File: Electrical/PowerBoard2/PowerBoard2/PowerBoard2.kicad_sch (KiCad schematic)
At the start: 10 parts, among them J1 XT60PW-M, J2 XT60PW-M, J3 B4B-XH-A_LF__SN_, J5 XT60PW-M, U2 INA226AIDGSR, U3 USB-A-S-RA-TSMT

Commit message: pullup resistors
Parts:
- R3, R4: footprint (none) -> Resistor_SMD:R_0805_2012Metric_Pad1.20x1.40mm_HandSolder
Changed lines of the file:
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@@
 			)
 		)
-		(property "Footprint" ""
+		(property "Footprint" "Resistor_SMD:R_0805_2012Metric_Pad1.20x1.40mm_HandSolder"
 			(at 58.42 90.678 90)
 			(effects
@@
 			)
 		)
-		(property "Footprint" ""
+		(property "Footprint" "Resistor_SMD:R_0805_2012Metric_Pad1.20x1.40mm_HandSolder"
 			(at 58.42 85.598 90)
 			(effects

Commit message: widened traces for 5V output
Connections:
- net +3.3V: now reaches J3.1, R3.1, R4.1, U2.6 (VS)
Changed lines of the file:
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@@
+	)
+	(junction
+		(at 123.19 74.93)
+		(diameter 0)
+		(color 0 0 0 0)
 	)
 	(junction
@@
 	(wire
 		(pts
+			(xy 123.19 74.93) (xy 111.76 74.93)
+		)
+		(stroke
+			(width 0)
+			(type default)
+		)
+	)
+	(wire
+		(pts
 			(xy 104.14 68.58) (xy 114.3 68.58)
 		)
@@
 	(wire
 		(pts
-			(xy 128.27 74.93) (xy 111.76 74.93)
+			(xy 128.27 74.93) (xy 123.19 74.93)
 		)
 		(stroke
@@
 					(unit 1)
 				)
+			)
+		)
+	)
+	(symbol
+		(lib_id "power:+3.3V")
+		(at 123.19 74.93 0)
+		(unit 1)
+		(exclude_from_sim no)
+		(in_bom yes)
+		(on_board yes)
+		(dnp no)
+		(fields_autoplaced yes)
+		(property "Reference" "#PWR011"
+			(at 123.19 78.74 0)
+			(effects
+				(font
+					(size 1.27 1.27)
+				)
+				(hide yes)
+			)
+		)
+		(property "Value" "+3.3V"
+			(at 123.19 69.85 0)
+			(effects
+				(font
+					(size 1.27 1.27)
+				)
+			)
+		)
+		(property "Footprint" ""
+			(at 123.19 74.93 0)
+			(effects
+				(font
+					(size 1.27 1.27)
+				)
+				(hide yes)
+			)
+		)
+		(property "Datasheet" ""
+			(at 123.19 74.93 0)
+			(effects
+				(font
+					(size 1.27 1.27)
+				)
+				(hide yes)
+			)
+		)
+		(property "Description" "Power symbol creates a global label with name \"+3.3V\""
+			(at 123.19 74.93 0)
+			(effects
+				(font
+					(size 1.27 1.27)
+				)
+				(hide yes)
+			)
+		)
+		(pin "1"
+		)
+		(instances
+			(project ""
+				(path "/f95f296f-a4bf-4952-bdc7-66087a6cc347"
+					(reference "#PWR011")
+					(unit 1)
+				)

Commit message: stabilizing capacitors
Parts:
- added C3: 100uF, Capacitor_SMD:C_0805_2012Metric_Pad1.18x1.45mm_HandSolder, symbol Device:C
- added C6: 10uF, Capacitor_SMD:C_0805_2012Metric_Pad1.18x1.45mm_HandSolder, symbol Device:C
- added C7: 0.1uF, Capacitor_SMD:C_0805_2012Metric_Pad1.18x1.45mm_HandSolder, symbol Device:C
- C2: value 300uF -> 100uF
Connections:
- net +5V: now also C3.1, C6.1, C7.1
- net GND: now also C3.2, C6.2, C7.2

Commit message: bypass capacitor
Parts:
- added C8: 0.1uF, Capacitor_SMD:C_0805_2012Metric_Pad1.18x1.45mm_HandSolder, symbol Device:C
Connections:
- net +3.3V: now also C8.1
- net GND: now also C8.2
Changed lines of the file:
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@@
+	)
+	(junction
+		(at 106.68 66.04)
+		(diameter 0)
+		(color 0 0 0 0)
 	)
 	(junction
@@
 	(wire
 		(pts
+			(xy 106.68 55.88) (xy 106.68 58.42)
+		)
+		(stroke
+			(width 0)
+			(type default)
+		)
+	)
+	(wire
+		(pts
 			(xy 64.77 83.82) (xy 64.77 102.87)
 		)
@@
 	(wire
 		(pts
-			(xy 104.14 68.58) (xy 114.3 68.58)
+			(xy 104.14 68.58) (xy 119.38 68.58)
 		)
 		(stroke
@@
 	(wire
 		(pts
-			(xy 111.76 66.04) (xy 104.14 66.04)
+			(xy 111.76 66.04) (xy 106.68 66.04)
 		)
 		(stroke
@@
 	(wire
 		(pts
-			(xy 114.3 53.34) (xy 54.61 53.34)
+			(xy 119.38 53.34) (xy 54.61 53.34)
 		)
 		(stroke
@@
 	(wire
 		(pts
-			(xy 114.3 68.58) (xy 114.3 53.34)
+			(xy 119.38 68.58) (xy 119.38 53.34)
 		)
 		(stroke
@@
 		(pts
 			(xy 101.6 118.11) (xy 101.6 124.46)
+		)
+		(stroke
+			(width 0)
+			(type default)
+		)
+	)
+	(wire
+		(pts
+			(xy 106.68 66.04) (xy 104.14 66.04)
 		)
 		(stroke
@@
 	)
 	(symbol
+		(lib_id "Device:C")
+		(at 106.68 62.23 180)
+		(unit 1)
+		(exclude_from_sim no)
+		(in_bom yes)
+		(on_board yes)
+		(dnp no)
+		(fields_autoplaced yes)
+		(property "Reference" "C8"
+			(at 110.49 60.9599 0)
+			(effects
+				(font
+					(size 1.27 1.27)
+				)
+				(justify right)
+			)
+		)
+		(property "Value" "0.1uF"
+			(at 110.49 63.4999 0)
+			(effects
+				(font
+					(size 1.27 1.27)
+				)
+				(justify right)
+			)
+		)
+		(property "Footprint" "Capacitor_SMD:C_0805_2012Metric_Pad1.18x1.45mm_HandSolder"
+			(at 105.7148 58.42 0)
+			(effects
+				(font
+					(size 1.27 1.27)
+				)
+				(hide yes)
+			)
+		)
+		(property "Datasheet" "~"
+			(at 106.68 62.23 0)
+			(effects
+				(font
+					(size 1.27 1.27)
+				)
+				(hide yes)
+			)
+		)
+		(property "Description" "Unpolarized capacitor"
+			(at 106.68 62.23 0)
+			(effects
+				(font
+					(size 1.27 1.27)
+				)
+				(hide yes)
+			)
+		)
+		(pin "2"
+		)
+		(pin "1"
+		)
+		(instances
+			(project "PowerBoard2"
+				(path "/f95f296f-a4bf-4952-bdc7-66087a6cc347"
+					(reference "C8")
+					(unit 1)
+				)
+			)
+		)
+	)
+	(symbol
 		(lib_id "power:GND")
 		(at 40.64 63.5 0)
@@
 					(unit 1)
 				)
+			)
+		)
+	)
+	(symbol
+		(lib_id "power:GND")
+		(at 106.68 55.88 270)
+		(unit 1)
+		(exclude_from_sim no)
+		(in_bom yes)
+		(on_board yes)
+		(dnp no)
+		(fields_autoplaced yes)
+		(property "Reference" "#PWR012"
+			(at 100.33 55.88 0)
+			(effects
+				(font
+					(size 1.27 1.27)
+				)
+				(hide yes)
+			)
+		)
+		(property "Value" "GND"
+			(at 102.87 55.8799 90)
+			(effects
+				(font
+					(size 1.27 1.27)
+				)
+				(justify right)
+			)
+		)
+		(property "Footprint" ""
+			(at 106.68 55.88 0)
+			(effects
+				(font
+					(size 1.27 1.27)
+				)
+				(hide yes)
+			)
+		)
+		(property "Datasheet" ""
+			(at 106.68 55.88 0)
+			(effects
+				(font
+					(size 1.27 1.27)
+				)
+				(hide yes)
+			)
+		)
+		(property "Description" "Power symbol creates a global label with name \"GND\" , ground"
+			(at 106.68 55.88 0)
+			(effects
+				(font
+					(size 1.27 1.27)
+				)
+				(hide yes)
+			)
+		)
+		(pin "1"
+		)
+		(instances
+			(project ""
+				(path "/f95f296f-a4bf-4952-bdc7-66087a6cc347"
+					(reference "#PWR012")
+					(unit 1)
+				)

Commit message: shunt
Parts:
- removed ShuntResistor1: 0.005 R, Resistor_SMD:R_2010_5025Metric_Pad1.40x2.65mm_HandSolder, symbol Device:R
- added R5: CSNL2010FT2L00, Shuntresistor:STA_CSNL2010&lessthan_=3_STP, symbol 2025-05-07_20-00-53:CSNL2010FT2L00
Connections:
- net +12V: now also R5.1
- net Buck Converter/Vin (12V): now also R5.2
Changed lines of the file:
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@@
-	)
-	(junction
-		(at 43.18 76.2)
-		(diameter 0)
-		(color 0 0 0 0)
 	)
 	(junction
@@
 	)
 	(junction
+		(at 43.18 73.66)
+		(diameter 0)
+		(color 0 0 0 0)
+	)
+	(junction
 		(at 135.89 160.02)
 		(diameter 0)
@@
 	)
 	(junction
-		(at 43.18 83.82)
-		(diameter 0)
-		(color 0 0 0 0)
-	)
-	(junction
 		(at 110.49 138.43)
 		(diameter 0)
@@
 		(color 0 0 0 0)
 	)
+	(junction
+		(at 43.18 86.36)
+		(diameter 0)
+		(color 0 0 0 0)
+	)
 	(no_connect
 		(at 99.06 168.91)
@@
 	(wire
 		(pts
-			(xy 45.72 76.2) (xy 43.18 76.2)
+			(xy 45.72 73.66) (xy 43.18 73.66)
 		)
 		(stroke
@@
 	(wire
 		(pts
-			(xy 43.18 83.82) (xy 45.72 83.82)
+			(xy 45.72 86.36) (xy 43.18 86.36)
 		)
 		(stroke
@@
 	(wire
 		(pts
-			(xy 45.72 83.82) (xy 45.72 81.28)
+			(xy 45.72 86.36) (xy 45.72 81.28)
 		)
 		(stroke
@@
 	(wire
 		(pts
-			(xy 43.18 83.82) (xy 43.18 113.03)
+			(xy 43.18 86.36) (xy 43.18 113.03)
 		)
 		(stroke
@@
 	(wire
 		(pts
-			(xy 43.18 72.39) (xy 43.18 76.2)
+			(xy 43.18 72.39) (xy 43.18 73.66)
 		)
 		(stroke
@@
 	(wire
 		(pts
-			(xy 45.72 78.74) (xy 45.72 76.2)
+			(xy 45.72 78.74) (xy 45.72 73.66)
 		)
 		(stroke
@@
 	)
 	(symbol
-		(lib_id "Device:R")
-		(at 43.18 80.01 180)
+		(lib_id "2025-05-07_20-00-53:CSNL2010FT2L00")
+		(at 43.18 73.66 270)
 		(unit 1)
 		(exclude_from_sim no)
@@
 		(on_board yes)
 		(dnp no)
-		(property "Reference" "ShuntResistor1"
-			(at 40.894 80.518 0)
-			(effects
-				(font
-					(size 1.27 1.27)
+		(property "Reference" "R5"
+			(at 38.1 79.248 90)
+			(effects
+				(font
+					(size 1.524 1.524)
 				)
 				(justify left)
 			)
 		)
-		(property "Value" "0.005 R"
-			(at 37.846 78.486 0)
-			(effects
-				(font
-					(size 1.27 1.27)
+		(property "Value" "CSNL2010FT2L00"
+			(at 21.59 81.2799 90)
+			(effects
+				(font
+					(size 1.524 1.524)
 				)
 				(justify left)
 			)
 		)
-		(property "Footprint" "Resistor_SMD:R_2010_5025Metric_Pad1.40x2.65mm_HandSolder"
-			(at 44.958 80.01 90)
-			(effects
-				(font
-					(size 1.27 1.27)
-				)
-				(hide yes)
-			)
-		)
-		(property "Datasheet" "~"
-			(at 43.18 80.01 0)
-			(effects
-				(font
-					(size 1.27 1.27)
-				)
-				(hide yes)
-			)
-		)
-		(property "Description" "Resistor"
-			(at 43.18 80.01 0)
-			(effects
-				(font
-					(size 1.27 1.27)
-				)
-				(hide yes)
-			)
+		(property "Footprint" "Shuntresistor:STA_CSNL2010&lessthan_=3_STP"
+			(at 43.18 73.66 0)
+			(effects
+				(font
+					(size 1.27 1.27)
+					(italic yes)
+				)
+				(hide yes)
+			)
+		)
+		(property "Datasheet" "CSNL2010FT2L00"
+			(at 43.18 73.66 0)
+			(effects
+				(font
+					(size 1.27 1.27)
+					(italic yes)
+				)
+				(hide yes)
+			)
+		)
+		(property "Description" ""
+			(at 43.18 73.66 0)
+			(effects
+				(font
+					(size 1.27 1.27)
+				)
+				(hide yes)
+			)
+		)
+		(pin "2"
 		)
 		(pin "1"
-		)
-		(pin "2"
 		)
 		(instances
 			(project ""
 				(path "/f95f296f-a4bf-4952-bdc7-66087a6cc347"
-					(reference "ShuntResistor1")
+					(reference "R5")
 					(unit 1)
 				)

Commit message: capacitors and opamps
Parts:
- removed C2, C3: 100uF, Capacitor_SMD:C_0805_2012Metric_Pad1.18x1.45mm_HandSolder, symbol Device:C
- added C2: 16ZLJ470MTA8X11.5, CAP_YX_8X11P5_RUB, symbol 2025-05-07_21-08-47:16ZLJ470MTA8X11.5
- added J4: B4B-XH-A_LF__SN_, B4B-XH-A_LF__SN_:JST_B4B-XH-A_LF__SN_, symbol B4B-XH-A_LF__SN_:B4B-XH-A_LF__SN_
- added R6: 36k, Resistor_SMD:R_0805_2012Metric_Pad1.20x1.40mm_HandSolder, symbol Device:R
- added R7, R9: 33k, Resistor_SMD:R_0805_2012Metric_Pad1.20x1.40mm_HandSolder, symbol Device:R
- added R8: 120k, Resistor_SMD:R_0805_2012Metric_Pad1.20x1.40mm_HandSolder, symbol Device:R
- added U4, U5: TLV2370IDBVR, DBV6, symbol 2025-02-22_17-10-12:TLV2370IDBVR
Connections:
- net +5V: now also C2.2, R6.1, U4.6 (VDD), U5.6 (VDD)
- net Buck Converter/Vin (12V): now also R8.1
- net GND: now also C2.1, J4.4, R7.2, R9.2, U4.2 (GND), U5.2 (GND)
- new net: J4.3, U5.1 (OUT), U5.4 (IN-)
- new net: R8.2, R9.1, U5.3 (IN+)
- new net: R6.2, R7.1, U4.3 (IN+)
- new net: J4.2, U4.1 (OUT), U4.4 (IN-)
- no-connect marks 3 -> 5

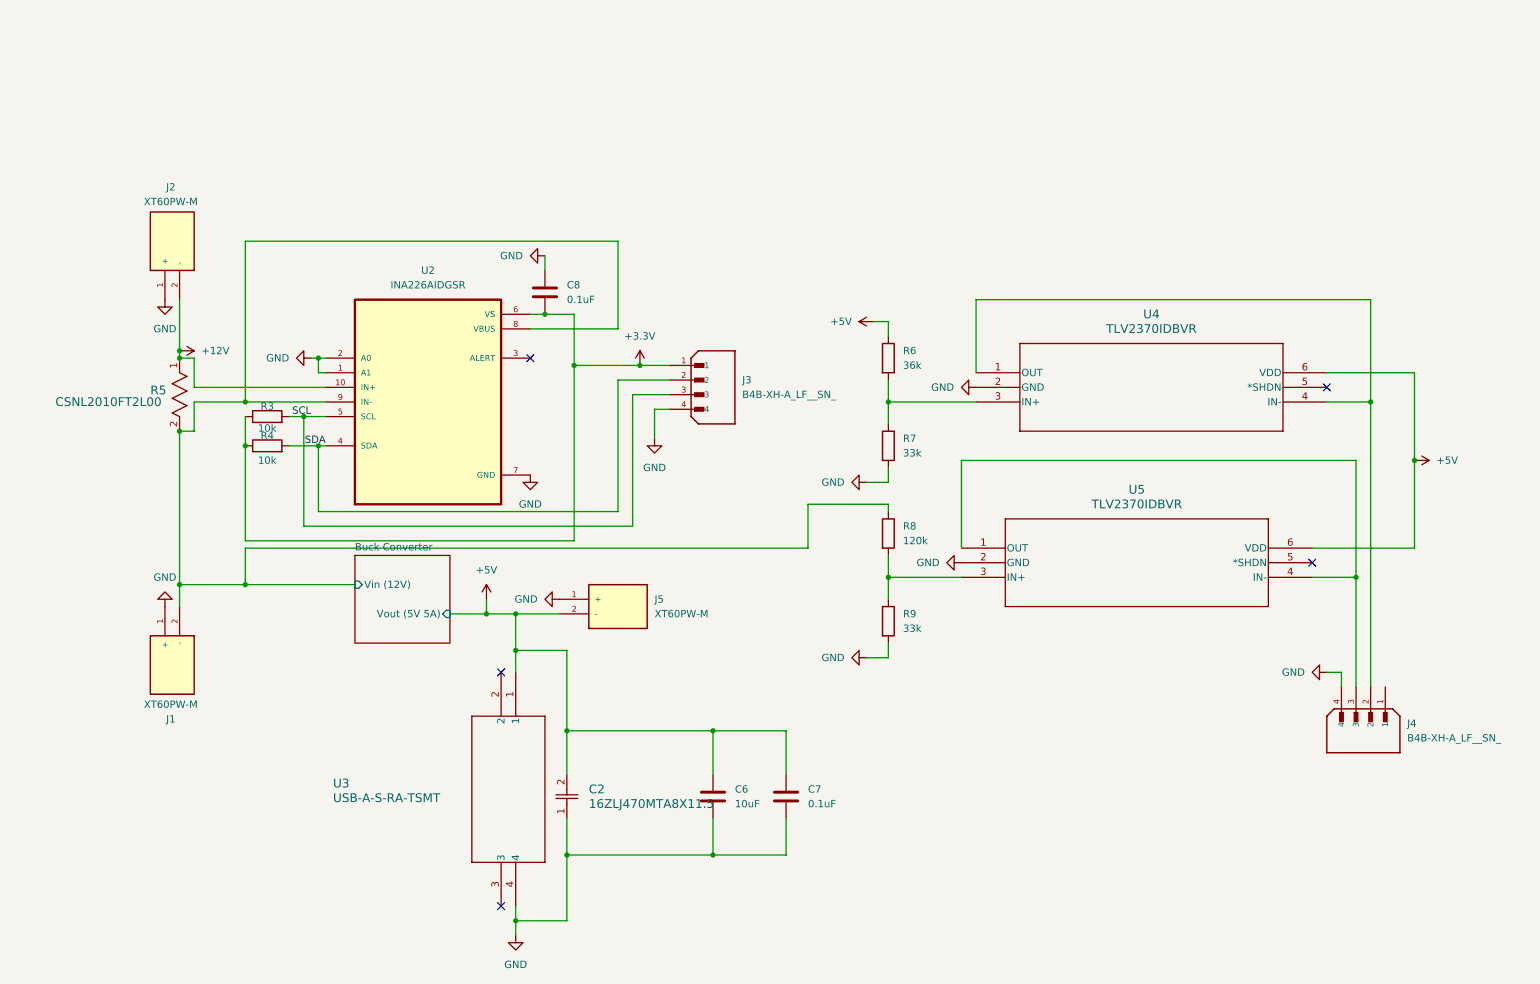
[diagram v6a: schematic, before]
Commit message: Updated Board to use two INA226
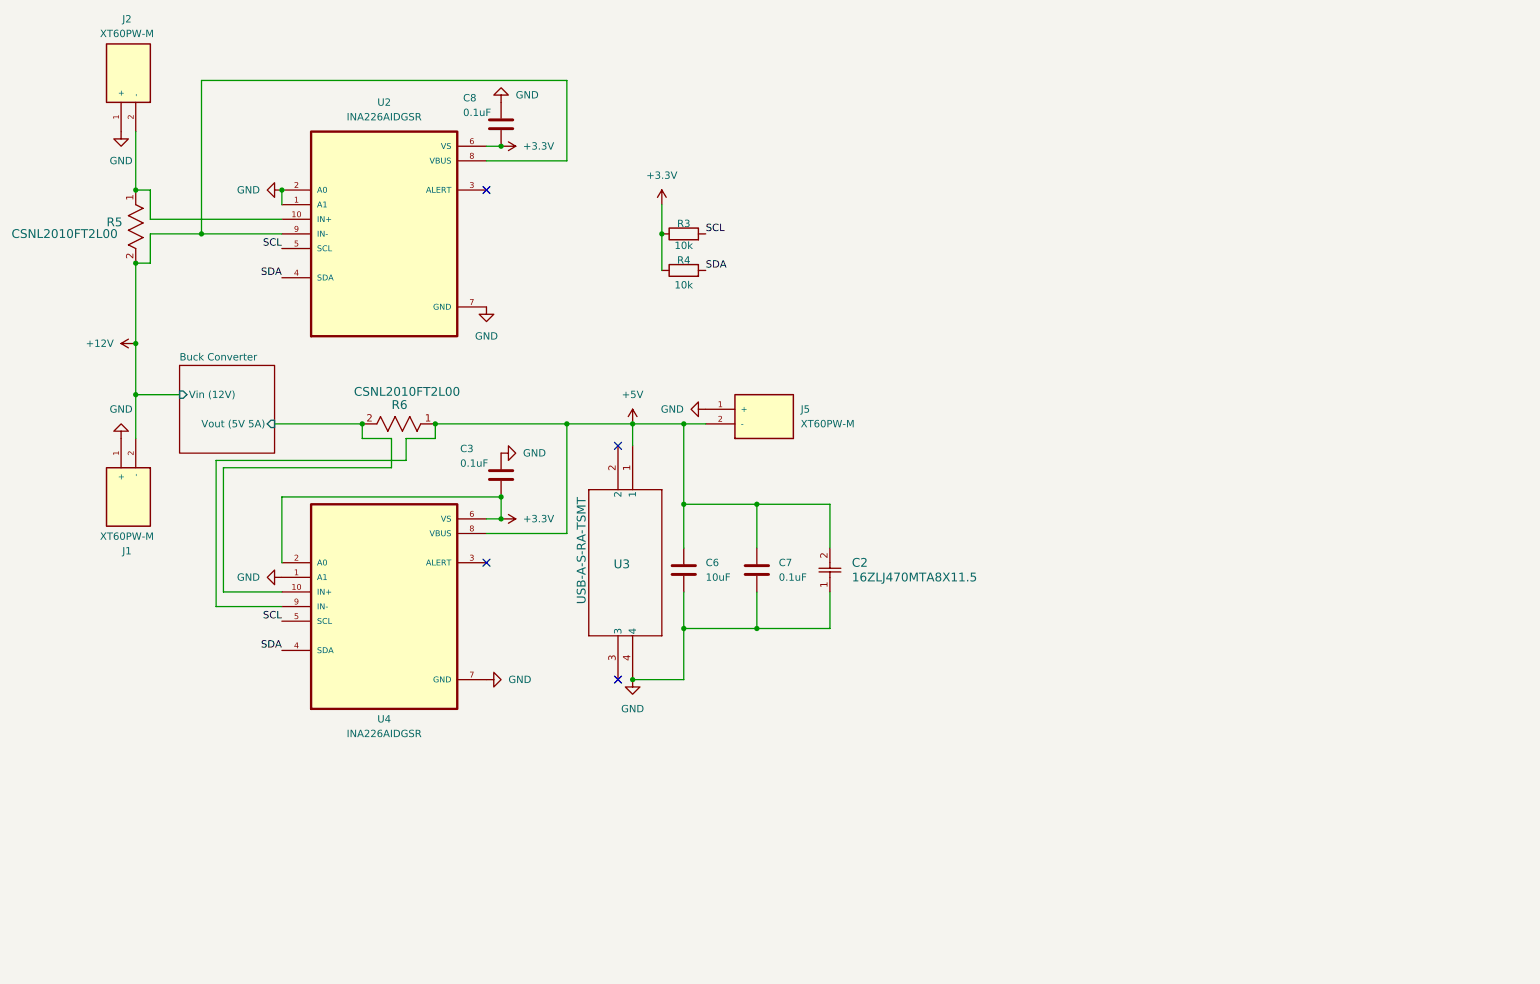
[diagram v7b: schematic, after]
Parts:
- removed J3, J4: B4B-XH-A_LF__SN_, B4B-XH-A_LF__SN_:JST_B4B-XH-A_LF__SN_, symbol B4B-XH-A_LF__SN_:B4B-XH-A_LF__SN_
- removed R6: 36k, Resistor_SMD:R_0805_2012Metric_Pad1.20x1.40mm_HandSolder, symbol Device:R
- removed R7, R9: 33k, Resistor_SMD:R_0805_2012Metric_Pad1.20x1.40mm_HandSolder, symbol Device:R
- removed R8: 120k, Resistor_SMD:R_0805_2012Metric_Pad1.20x1.40mm_HandSolder, symbol Device:R
- removed U4, U5: TLV2370IDBVR, DBV6, symbol 2025-02-22_17-10-12:TLV2370IDBVR
- added C3: 0.1uF, Capacitor_SMD:C_0805_2012Metric_Pad1.18x1.45mm_HandSolder, symbol Device:C
- added R6: CSNL2010FT2L00, Shuntresistor:STA_CSNL2010&lessthan_=3_STP, symbol 2025-05-07_20-00-53:CSNL2010FT2L00
- added U4: INA226AIDGSR, Libraries:INA226AIDGSR, symbol INA226AIDGSR:INA226AIDGSR
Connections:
- net Buck Converter/Vin (12V) is gone; now on net +12V: J1.2 (-), R5.2, U2.8 (VBUS), U2.9 (IN-)
- net +12V: no longer J2.2 (-), R5.1, U2.10 (IN+)
- net +3.3V: now also C3.1, U4.2 (A0), U4.6 (VS)
- net +5V: now also R6.1, U4.8 (VBUS), U4.9 (IN-)
- net GND: now also C3.2, U4.1 (A1), U4.7 (GND)
- net SCL: now also U4.5 (SCL)
- net SDA: now also U4.4 (SDA)
- new net: J2.2 (-), R5.1, U2.10 (IN+)
- new net Buck Converter/Vout (5V 5A): R6.2, U4.10 (IN+)
- no-connect marks 5 -> 4
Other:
- moved on the sheet: C2, C6, C7, C8, J1, J2, J5, R3, R4, R5, U2, U3
